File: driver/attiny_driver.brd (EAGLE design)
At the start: 160 x 100 mm, 10 parts, among them IC1 ATTiny85, IC4 LB1973M, J1 AVR_SPI_PRG_6NS

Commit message: routed
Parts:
- moved C1 42.9 mm to (11.2, 11.4)
- moved C2 42.9 mm to (11.8, 17.8)
- moved IC1 42.9 mm to (15.0, 5.71)
- moved IC2 42.9 mm to (14.4, 17.8)
- moved IC4 42.9 mm to (13.1, 17.8)
- moved J1 42.9 mm to (6.73, 10.8)
- moved JP1 42.9 mm to (18.2, 11.4)
- moved JP2 42.9 mm to (19.4, 17.8)
- moved JP3 42.9 mm to (6.73, 17.8)
- moved LED1 42.9 mm to (11.2, 9.53)
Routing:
- net +5V: track 0.00 -> 28.3 mm, vias 0 -> 1
- net SDA/MOSI: track 0.00 -> 25.4 mm, vias 0 -> 1
- net IN1/MISO: track 0.00 -> 22.4 mm, vias 0 -> 1
- net IN3: track 0.00 -> 20.6 mm, vias 0 -> 1
- net N$6: track 0.00 -> 20.1 mm, vias 0 -> 1
- net SCL/SCK: track 0.00 -> 15.1 mm
- net OUT2: track 0.00 -> 10.2 mm
- net OUT4: track 0.00 -> 9.72 mm
- net N$3: track 0.00 -> 8.32 mm, vias 0 -> 1
- net OUT1: track 0.00 -> 7.54 mm
- net OUT3: track 0.00 -> 6.81 mm
- net IN2: track 0.00 -> 3.07 mm, vias 0 -> 1
- net IN4: track 0.00 -> 3.01 mm, vias 0 -> 1
- net GND: track 0.00 -> 0.64 mm, vias 0 -> 9
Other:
- board size 160 x 100 mm -> 22 x 22 mm

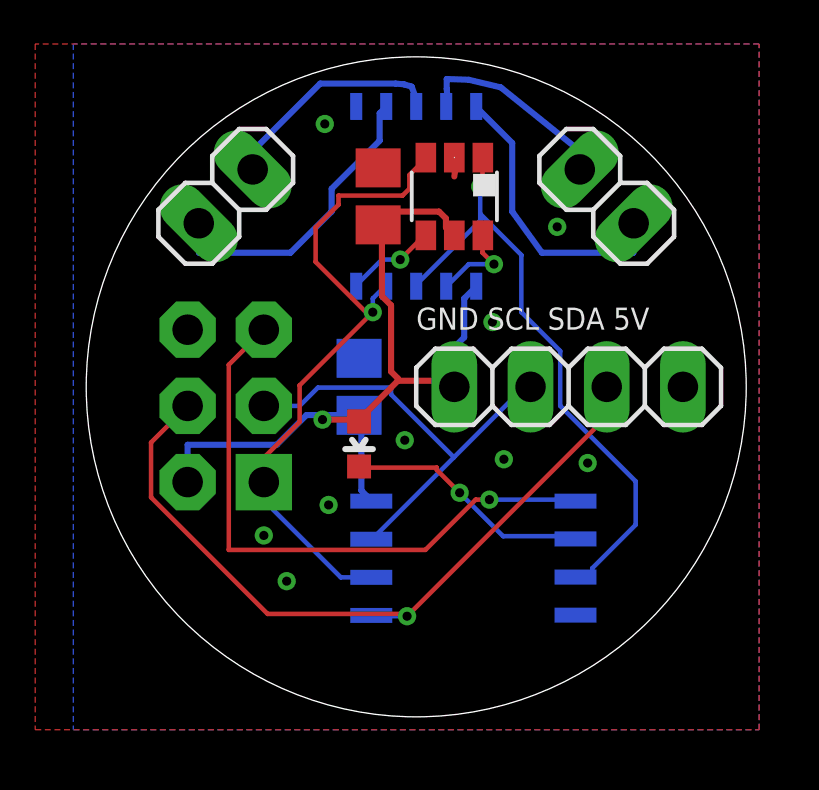
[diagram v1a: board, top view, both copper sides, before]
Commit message: stopmask around the edges to allow grounding to the metal tube this and the aircore itself go into
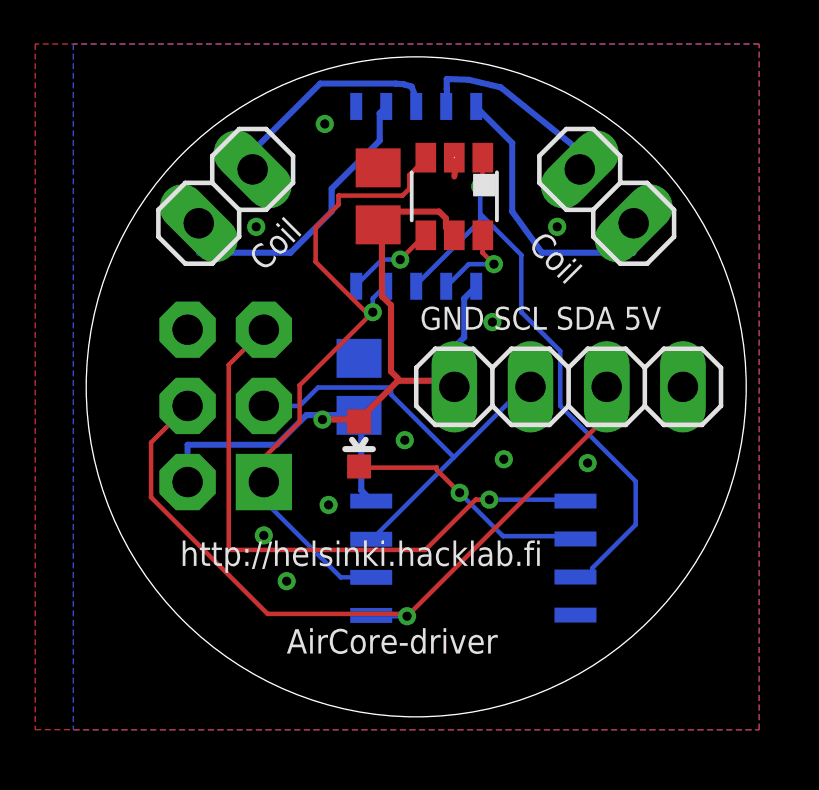
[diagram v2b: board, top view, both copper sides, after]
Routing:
- net GND: vias 9 -> 10
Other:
- board text added: "AirCore-driver"
- board text added: "Coil"
- board text added: "http://helsinki.hacklab.fi"
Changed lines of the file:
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@@
 <setting verticaltext="up"/>
 </settings>
-<grid distance="5" unitdist="mil" unit="mil" style="lines" multiple="1" display="no" altdistance="0.025" altunitdist="inch" altunit="inch"/>
+<grid distance="5" unitdist="mil" unit="mm" style="lines" multiple="1" display="no" altdistance="0.025" altunitdist="inch" altunit="inch"/>
 <layers>
 <layer number="1" name="Top" color="4" fill="1" visible="yes" active="yes"/>
@@
 <layer number="27" name="tValues" color="7" fill="1" visible="yes" active="yes"/>
 <layer number="28" name="bValues" color="7" fill="1" visible="yes" active="yes"/>
-<layer number="29" name="tStop" color="7" fill="3" visible="no" active="yes"/>
+<layer number="29" name="tStop" color="7" fill="3" visible="yes" active="yes"/>
 <layer number="30" name="bStop" color="7" fill="6" visible="no" active="yes"/>
 <layer number="31" name="tCream" color="7" fill="4" visible="no" active="yes"/>
@@
 <plain>
 <circle x="13.081" y="11.43" radius="11" width="0.01" layer="20"/>
-<text x="13.081" y="13.335" size="0.7366" layer="25" font="vector" ratio="11">GND SCL SDA 5V</text>
+<text x="13.208" y="13.335" size="0.762" layer="25" font="vector" ratio="14">GND SCL SDA 5V</text>
+<text x="5.207" y="5.461" size="0.8128" layer="21" font="vector" ratio="12">http://helsinki.hacklab.fi</text>
+<text x="8.763" y="2.54" size="0.8128" layer="21" font="vector" ratio="12">AirCore-driver</text>
+<text x="8.001" y="15.24" size="0.8128" layer="21" font="vector" ratio="12" rot="R45">Coil</text>
+<text x="18.669" y="15.367" size="0.8128" layer="21" font="vector" ratio="12" rot="R135">Coil</text>
+<circle x="13.1" y="11.4" radius="10.8" width="1.4224" layer="29"/>
+<circle x="13.1" y="11.4" radius="10.8" width="1.4224" layer="30"/>
 </plain>
 <attributes>
@@
 <via x="8.001" y="6.477" extent="1-16" drill="0.3048"/>
 <via x="10.16" y="7.493" extent="1-16" drill="0.3048"/>
+<via x="7.747" y="16.764" extent="1-16" drill="0.3048"/>
 </signal>
 <signal name="+5V" class="1">
